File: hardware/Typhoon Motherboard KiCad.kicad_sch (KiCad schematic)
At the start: 38 parts, among them J1 Conn_01x04_Pin, J10 USB_C_Receptacle_USB2.0, J2 Conn_02x03_Odd_Even, J3 Conn_01x04_Pin, U1 ESP32-S3-WROOM-1, U2 SN65HVD233, U7 MCP1825S

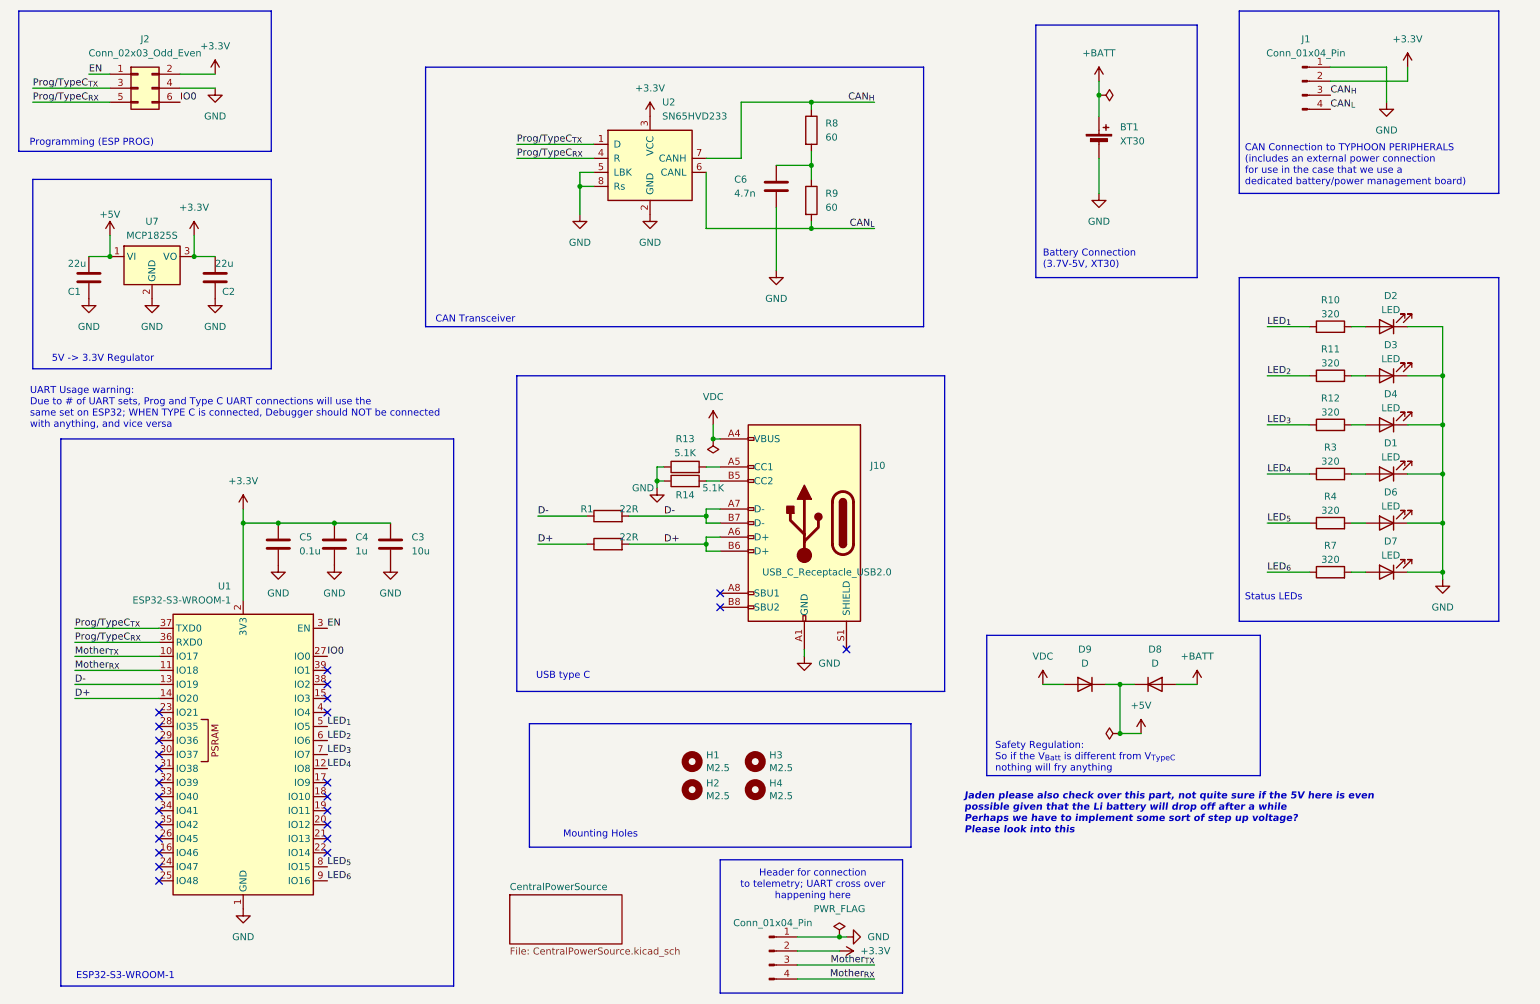
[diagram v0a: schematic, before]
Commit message: Updated the Boost Converter
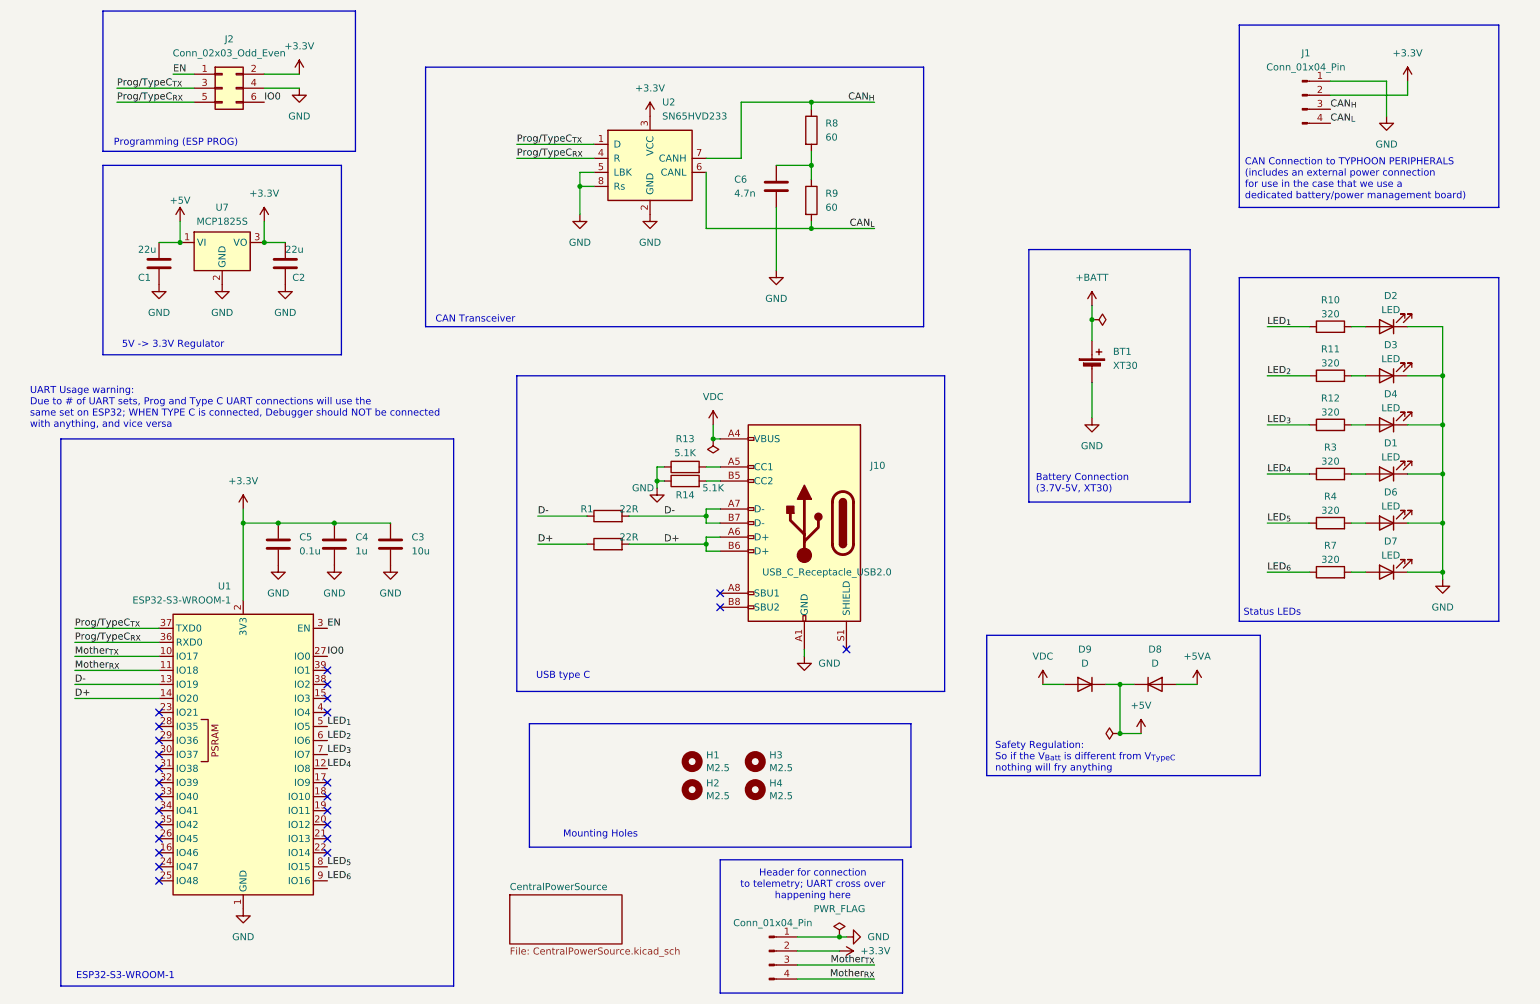
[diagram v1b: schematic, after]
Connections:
- net +BATT: no longer D8.2 (A)
- new net +5VA: D8.2 (A)
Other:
- note removed: "Jaden please also check over this part, not quite sure if the 5V here is even possible given that the Li battery will drop off after a while Perhaps we have to implement some sort of step up voltage? Please look into this"
- moved on the sheet: BT1, C1, C2, J1, J2, U7

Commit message: Production Files
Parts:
- removed D8, D9: D, Diode_SMD:D_SOD-123, symbol Device:D
- added D8, D9: D_Schottky, Diode_SMD:D_SOD-123, symbol Device:D_Schottky
- R1, R2: value 22R -> 22
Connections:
- net +5V: now also D8.1 (K), D9.1 (K)
- net +5VA: now also D9.2 (A)
- net VDC: now also D8.2 (A)
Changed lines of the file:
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@@
 			)
 		)
-		(property "Value" "22R"
+		(property "Value" "22"
 			(at 124.46 110.49 90)
 			(effects
@@
 	)
 	(symbol
-		(lib_id "Device:D")
-		(at 219.71 137.16 0)
-		(unit 1)
-		(exclude_from_sim no)
-		(in_bom yes)
-		(on_board yes)
-		(dnp no)
-		(fields_autoplaced yes)
-		(property "Reference" "D8"
-			(at 219.71 130.81 0)
-			(effects
-				(font
-					(size 1.27 1.27)
-				)
-			)
-		)
-		(property "Value" "D"
-			(at 219.71 133.35 0)
-			(effects
-				(font
-					(size 1.27 1.27)
-				)
-			)
-		)
-		(property "Footprint" "Diode_SMD:D_SOD-123"
-			(at 219.71 137.16 0)
-			(effects
-				(font
-					(size 1.27 1.27)
-				)
-				(hide yes)
-			)
-		)
-		(property "Datasheet" "~"
-			(at 219.71 137.16 0)
-			(effects
-				(font
-					(size 1.27 1.27)
-				)
-				(hide yes)
-			)
-		)
-		(property "Description" "Diode"
-			(at 219.71 137.16 0)
-			(effects
-				(font
-					(size 1.27 1.27)
-				)
-				(hide yes)
-			)
-		)
-		(property "Sim.Device" "D"
-			(at 219.71 137.16 0)
-			(effects
-				(font
-					(size 1.27 1.27)
-				)
-				(hide yes)
-			)
-		)
-		(property "Sim.Pins" "1=K 2=A"
-			(at 219.71 137.16 0)
-			(effects
-				(font
-					(size 1.27 1.27)
-				)
-				(hide yes)
-			)
-		)
-		(pin "1"
-		)
-		(pin "2"
-		)
-		(instances
-			(project "Typhoon Motherboard KiCad"
-				(path "/13012fcd-02e9-4b82-8301-52da00f60a6e"
-					(reference "D8")
-					(unit 1)
-				)
-			)
-		)
-	)
-	(symbol
 		(lib_id "power:GND")
 		(at 60.96 115.57 0)
@@
 	)
 	(symbol
+		(lib_id "Device:D_Schottky")
+		(at 219.71 137.16 0)
+		(unit 1)
+		(exclude_from_sim no)
+		(in_bom yes)
+		(on_board yes)
+		(dnp no)
+		(fields_autoplaced yes)
+		(property "Reference" "D9"
+			(at 219.3925 130.81 0)
+			(effects
+				(font
+					(size 1.27 1.27)
+				)
+			)
+		)
+		(property "Value" "D_Schottky"
+			(at 219.3925 133.35 0)
+			(effects
+				(font
+					(size 1.27 1.27)
+				)
+			)
+		)
+		(property "Footprint" "Diode_SMD:D_SOD-123"
+			(at 219.71 137.16 0)
+			(effects
+				(font
+					(size 1.27 1.27)
+				)
+				(hide yes)
+			)
+		)
+		(property "Datasheet" "~"
+			(at 219.71 137.16 0)
+			(effects
+				(font
+					(size 1.27 1.27)
+				)
+				(hide yes)
+			)
+		)
+		(property "Description" "Schottky diode"
+			(at 219.71 137.16 0)
+			(effects
+				(font
+					(size 1.27 1.27)
+				)
+				(hide yes)
+			)
+		)
+		(pin "1"
+		)
+		(pin "2"
+		)
+		(instances
+			(project "Typhoon Motherboard KiCad"
+				(path "/13012fcd-02e9-4b82-8301-52da00f60a6e"
+					(reference "D9")
+					(unit 1)
+				)
+			)
+		)
+	)
+	(symbol
 		(lib_id "Mechanical:MountingHole")
 		(at 147.32 156.21 0)
@@
 	)
 	(symbol
+		(lib_id "Device:D_Schottky")
+		(at 207.01 137.16 180)
+		(unit 1)
+		(exclude_from_sim no)
+		(in_bom yes)
+		(on_board yes)
+		(dnp no)
+		(fields_autoplaced yes)
+		(property "Reference" "D8"
+			(at 207.3275 130.81 0)
+			(effects
+				(font
+					(size 1.27 1.27)
+				)
+			)
+		)
+		(property "Value" "D_Schottky"
+			(at 207.3275 133.35 0)
+			(effects
+				(font
+					(size 1.27 1.27)
+				)
+			)
+		)
+		(property "Footprint" "Diode_SMD:D_SOD-123"
+			(at 207.01 137.16 0)
+			(effects
+				(font
+					(size 1.27 1.27)
+				)
+				(hide yes)
+			)
+		)
+		(property "Datasheet" "~"
+			(at 207.01 137.16 0)
+			(effects
+				(font
+					(size 1.27 1.27)
+				)
+				(hide yes)
+			)
+		)
+		(property "Description" "Schottky diode"
+			(at 207.01 137.16 0)
+			(effects
+				(font
+					(size 1.27 1.27)
+				)
+				(hide yes)
+			)
+		)
+		(pin "1"
+		)
+		(pin "2"
+		)
+		(instances
+			(project "Typhoon Motherboard KiCad"
+				(path "/13012fcd-02e9-4b82-8301-52da00f60a6e"
+					(reference "D8")
+					(unit 1)
+				)
+			)
+		)
+	)
+	(symbol
 		(lib_id "power:GND")
 		(at 71.12 115.57 0)
@@
 	)
 	(symbol
-		(lib_id "Device:D")
-		(at 207.01 137.16 0)
-		(mirror y)
-		(unit 1)
-		(exclude_from_sim no)
-		(in_bom yes)
-		(on_board yes)
-		(dnp no)
-		(fields_autoplaced yes)
-		(property "Reference" "D9"
-			(at 207.01 130.81 0)
-			(effects
-				(font
-					(size 1.27 1.27)
-				)
-			)
-		)
-		(property "Value" "D"
-			(at 207.01 133.35 0)
-			(effects
-				(font
-					(size 1.27 1.27)
-				)
-			)
-		)
-		(property "Footprint" "Diode_SMD:D_SOD-123"
-			(at 207.01 137.16 0)
-			(effects
-				(font
-					(size 1.27 1.27)
-				)
-				(hide yes)
-			)
-		)
-		(property "Datasheet" "~"
-			(at 207.01 137.16 0)
-			(effects
-				(font
-					(size 1.27 1.27)
-				)
-				(hide yes)
-			)
-		)
-		(property "Description" "Diode"
-			(at 207.01 137.16 0)
-			(effects
-				(font
-					(size 1.27 1.27)
-				)
-				(hide yes)
-			)
-		)
-		(property "Sim.Device" "D"
-			(at 207.01 137.16 0)
-			(effects
-				(font
-					(size 1.27 1.27)
-				)
-				(hide yes)
-			)
-		)
-		(property "Sim.Pins" "1=K 2=A"
-			(at 207.01 137.16 0)
-			(effects
-				(font
-					(size 1.27 1.27)
-				)
-				(hide yes)
-			)
-		)
-		(pin "1"
-		)
-		(pin "2"
-		)
-		(instances
-			(project "Typhoon Motherboard KiCad"
-				(path "/13012fcd-02e9-4b82-8301-52da00f60a6e"
-					(reference "D9")
-					(unit 1)
-				)
-			)
-		)
-	)
-	(symbol
 		(lib_id "power:GND")
 		(at 115.57 52.07 0)
@@
 			)
 		)
-		(property "Value" "22R"
+		(property "Value" "22"
 			(at 124.46 105.41 90)
 			(effects
